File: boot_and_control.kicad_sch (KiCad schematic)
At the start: 44 parts, among them J2 Conn_ARM_JTAG_SWD_20, J3 Conn_01x06_Pin, J4 Conn_01x06_Pin, SW1 SW_DIP_x04, SW2 SW_DIP_x02, Y1 32.768k, Y2 24MHz

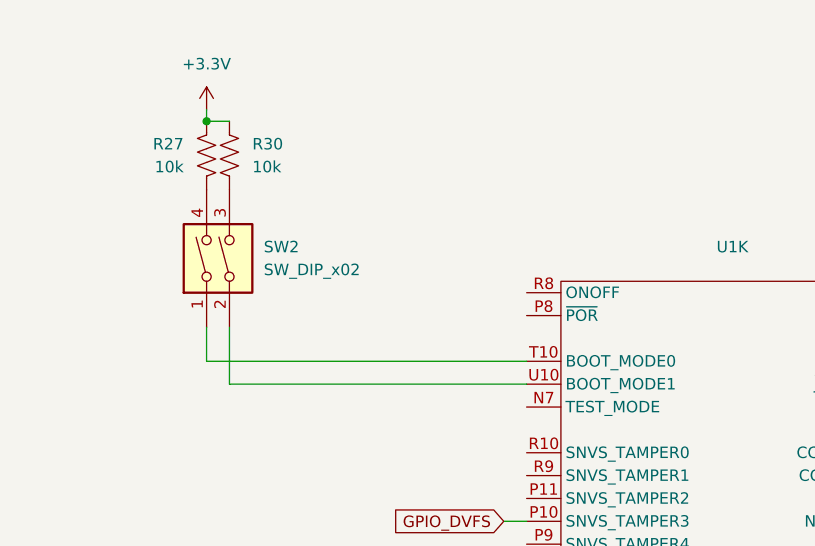
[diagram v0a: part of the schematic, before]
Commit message: Add in on-off switch, power-on reset controller
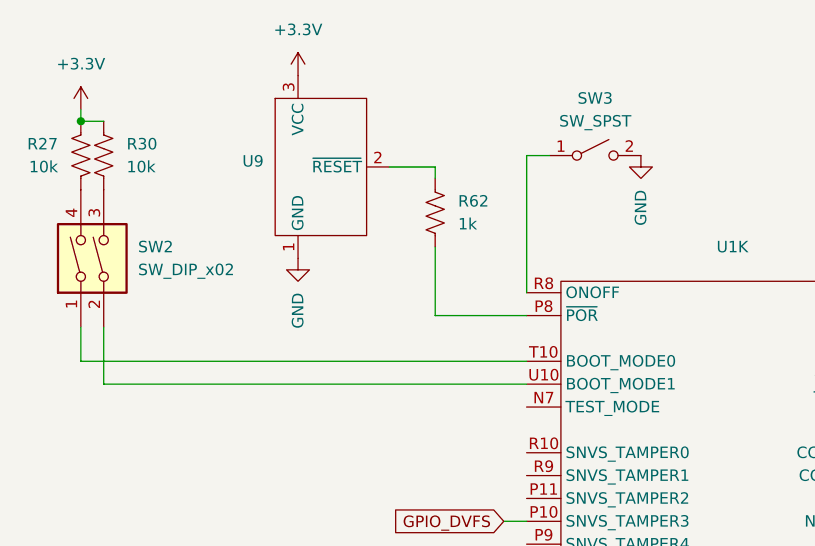
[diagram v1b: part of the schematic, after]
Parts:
- added R62: 1k, symbol Device:R_US
- added SW3: SW_SPST, Button_Switch_SMD:SW_SPST_Omron_B3FS-100xP, symbol Switch:SW_SPST
- added U9: ~, Package_TO_SOT_SMD:SOT-23-3, symbol imx6_test:UM803
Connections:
- net +3.3V: now also U9.3 (VCC)
- net GND: now also SW3.2 (B), U9.1 (GND)
- net at U1.P8 (~{POR}): now also R62.1
- net at U1.R8 (ONOFF): now also SW3.1 (A)
- new net: R62.2, U9.2 (~{RESET})
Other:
- moved on the sheet: R27, R30, SW2

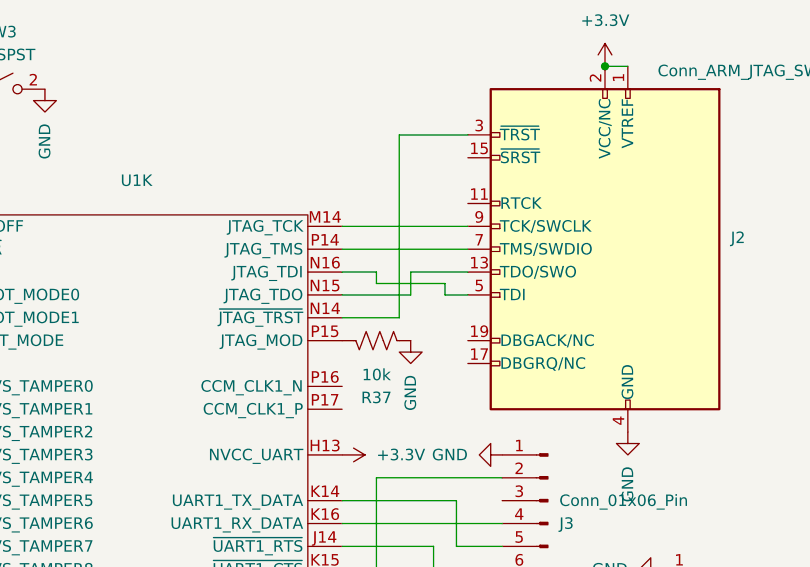
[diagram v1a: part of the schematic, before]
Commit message: Add in LCSC part numbers for major parts, assign packages
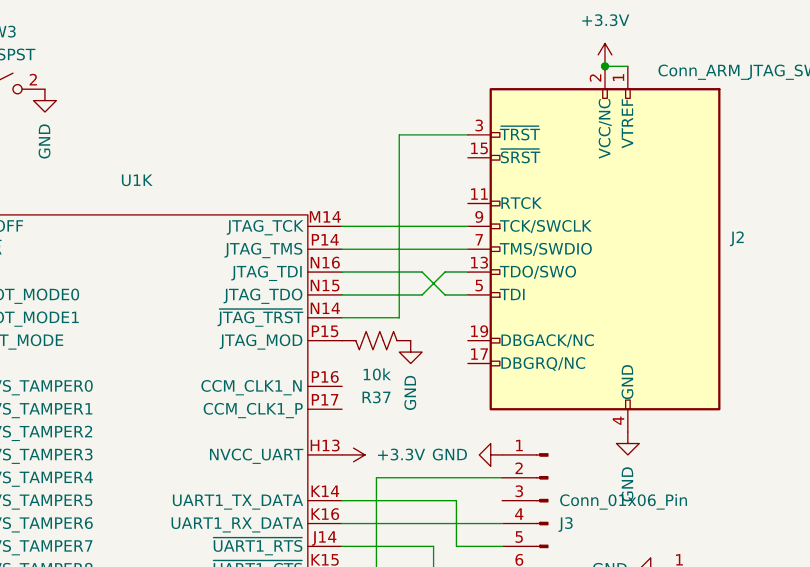
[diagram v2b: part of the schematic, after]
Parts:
- C56, C57, C58, C59, C60: footprint (none) -> Capacitor_SMD:C_0402_1005Metric
- J2: footprint (none) -> Connector_PinHeader_2.54mm:PinHeader_2x10_P2.54mm_Vertical
- J3, J4: footprint (none) -> Connector_PinHeader_2.54mm:PinHeader_1x06_P2.54mm_Vertical
- R26, R27, R28, R29, R30, R31, R32, R33, R34, R35, R36, R37, R38, R39, R40, R41, R42, R43, R44, R45, R46, R47, R48, R49, R50, R51, R54, R55, R56, R57, R61, R62: footprint (none) -> Resistor_SMD:R_0402_1005Metric
- U1: LCSC Part # (none) -> C414042
- U9: LCSC Part # (none) -> C620009
- Y1: LCSC Part # (none) -> C5366538
- Y2: LCSC Part # (none) -> C5807375
